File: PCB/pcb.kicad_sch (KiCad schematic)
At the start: 62 parts, among them J1 EXT POWER, J10 RGBW LED, J11 I2C Breakout, J2 Screw_Terminal_01x03, J3 RJ45, J4 RJ45, J5 EXT_BTN1, J6 EXT_BTN1, J7 Screw_Terminal_01x03, J8 Screw_Terminal_01x03, J9 Screw_Terminal_01x03, SW2 Factory Reset, SW3 User, SW4 User, U1 SN74LVC1G125DCK, U2 ADS1115IDGS, U4 AP63205WU, U5 AP2114-3.3, U6 LM358, U7 TJA1051T-3, U8 MOUDLE-SEEEDUINO-XIAO-ESP32S3

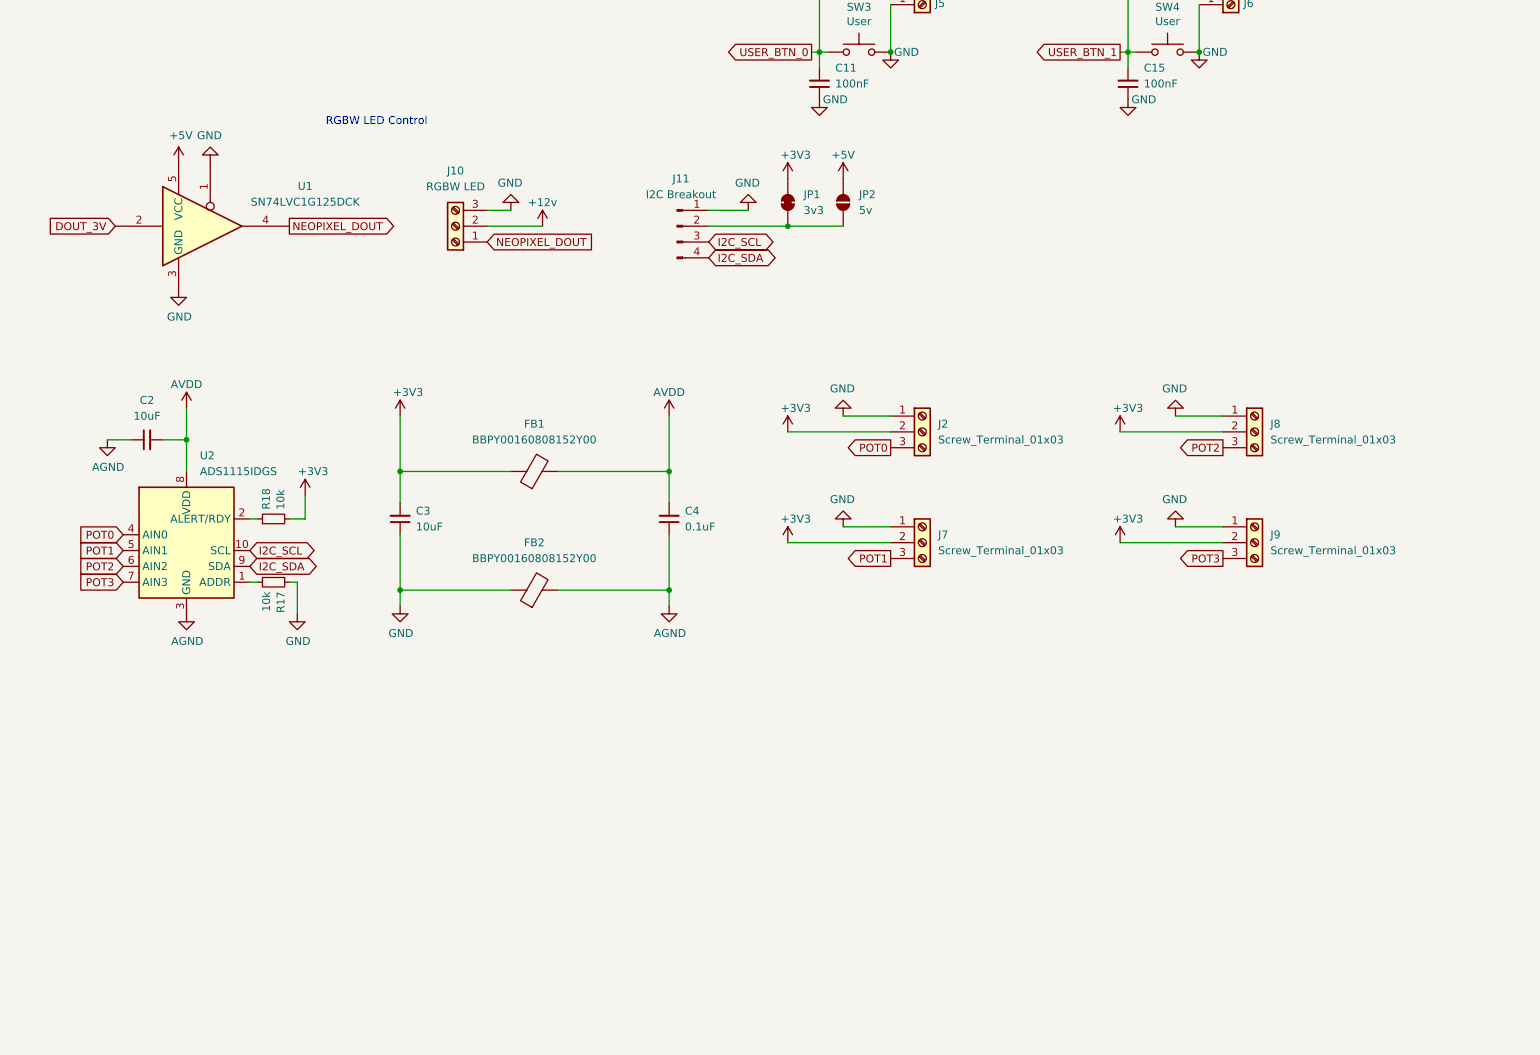
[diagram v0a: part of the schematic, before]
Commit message: Update PCB files with latest rev, export fabrication outputs, update README and add documentation photos
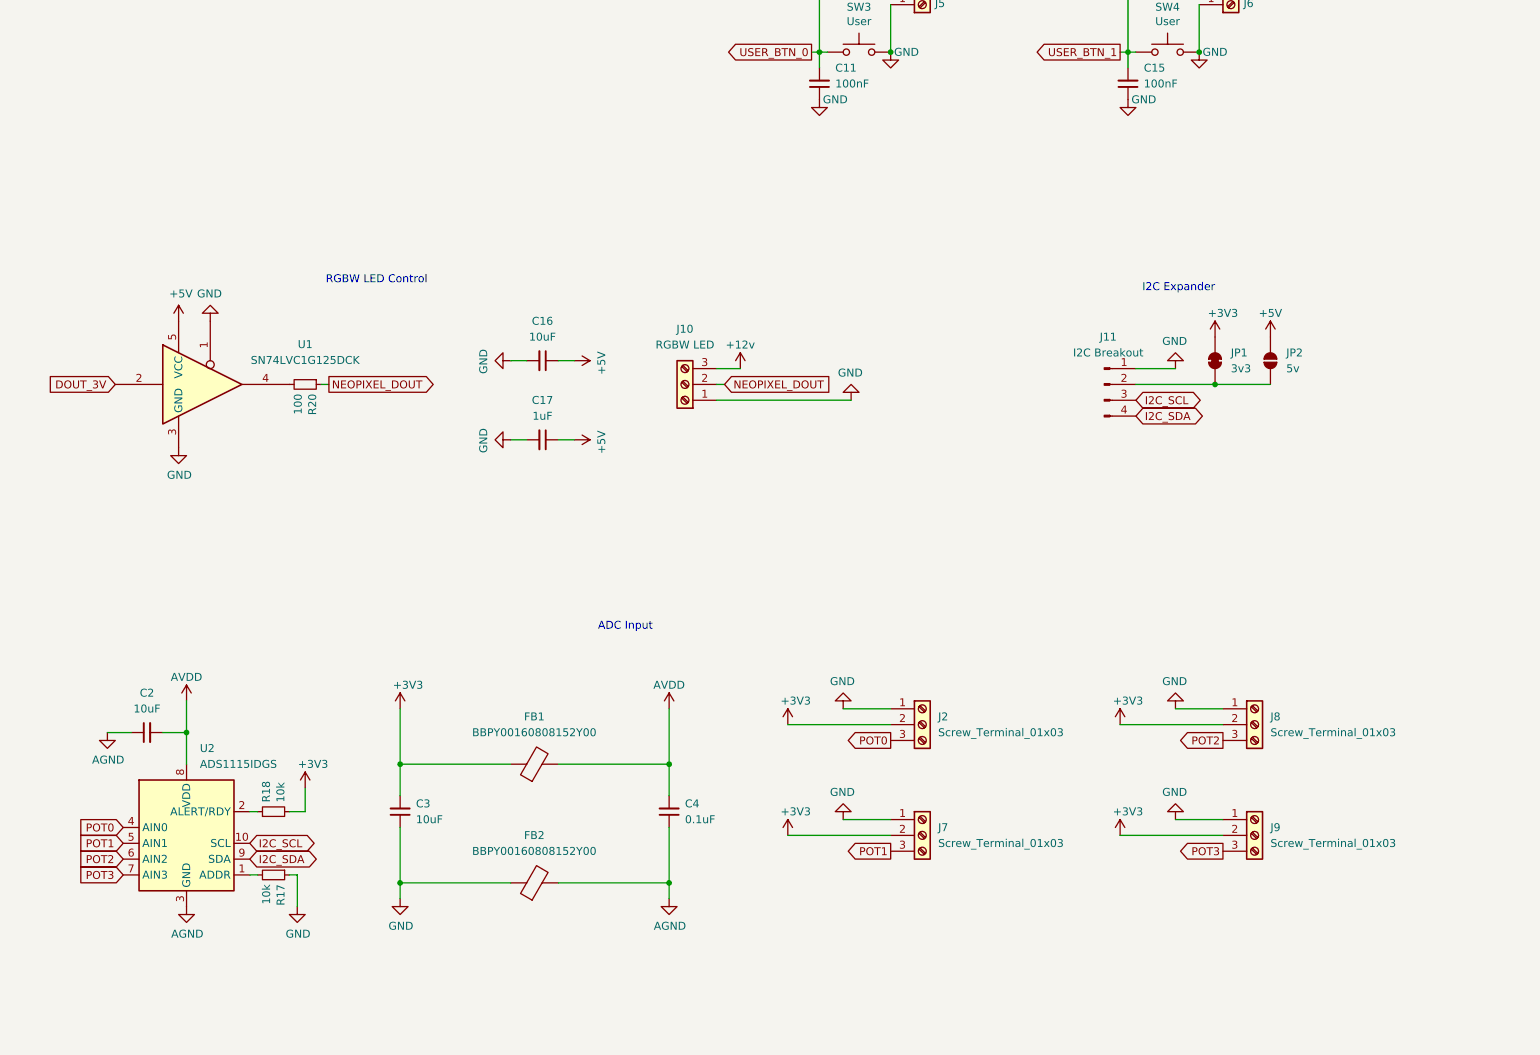
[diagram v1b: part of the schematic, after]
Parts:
- added C16: 10uF, Capacitor_SMD:C_0805_2012Metric_Pad1.18x1.45mm_HandSolder, symbol Device:C_Small
- added C17: 1uF, Capacitor_SMD:C_0805_2012Metric_Pad1.18x1.45mm_HandSolder, symbol Device:C_Small
- added R20: 100, Resistor_SMD:R_0603_1608Metric, symbol Device:R_Small
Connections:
- net +12v: now also J10.3 (Pin_3); no longer J10.2 (Pin_2)
- net +5V: now also C16.1, C17.1
- net GND: now also J10.1 (Pin_1), C16.2, C17.2; no longer J10.3 (Pin_3)
- net NEOPIXEL_DOUT: now also J10.2 (Pin_2), R20.1; no longer J10.1 (Pin_1), U1.4
- new net: R20.2, U1.4
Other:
- note added: "ADC Input"
- note added: "I2C Expander"
- moved on the sheet: C2, C3, C4, FB1, FB2, J10, J11, J2, J7, J8, J9, JP1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
